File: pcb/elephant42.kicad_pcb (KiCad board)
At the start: 2 copper layers, 139.8 x 201 mm, 155 parts, among them J1 MJ-4PP-9, J3 MJ-4PP-9, J4 Conn_01x01, SW1 SW_PUSH, SW10 SW_PUSH, SW11 SW_PUSH, SW12 SW_PUSH, SW13 SW_PUSH, SW14 SW_PUSH, SW15 SW_PUSH, SW16 SW_PUSH, SW17 SW_PUSH, SW18 SW_PUSH, SW19 SW_PUSH, SW2 SW_PUSH, SW20 SW_PUSH, SW21 SW_PUSH, SW22 SW_PUSH, SW23 SW_PUSH, SW24 SW_PUSH, SW25 SW_PUSH, SW26 SW_PUSH, SW27 SW_PUSH, SW28 SW_PUSH, SW29 SW_PUSH, SW3 SW_PUSH, SW30 SW_PUSH, SW31 SW_PUSH, SW32 SW_PUSH, SW33 SW_PUSH, SW34 SW_PUSH, SW35 SW_PUSH, SW36 SW_PUSH, SW37 SW_PUSH, SW38 SW_PUSH, SW39 SW_PUSH, SW4 SW_PUSH, SW40 SW_PUSH, SW41 SW_PUSH, SW42 SW_PUSH, SW5 SW_PUSH, SW6 SW_PUSH, SW7 SW_PUSH, SW8 SW_PUSH, SW9 SW_PUSH, U1 ProMicro, U2 ProMicro

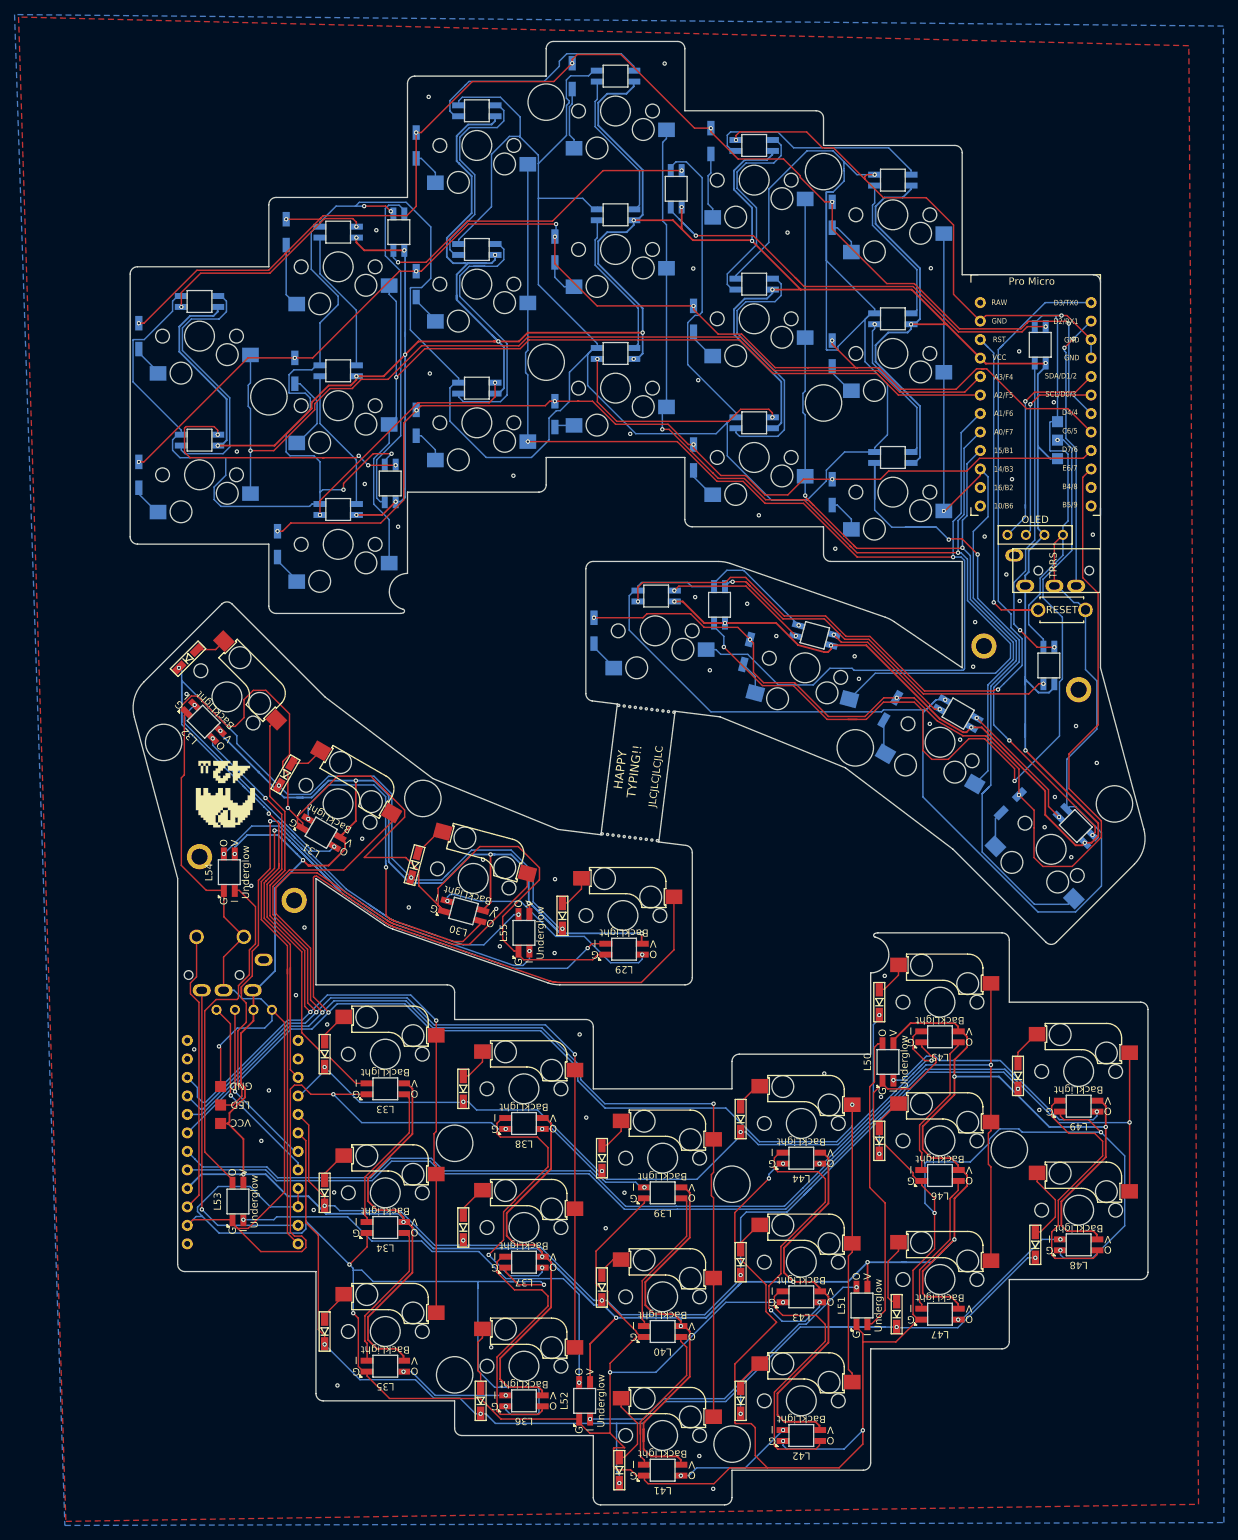
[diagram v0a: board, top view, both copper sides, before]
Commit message: Convert to choc hotswap with encoder
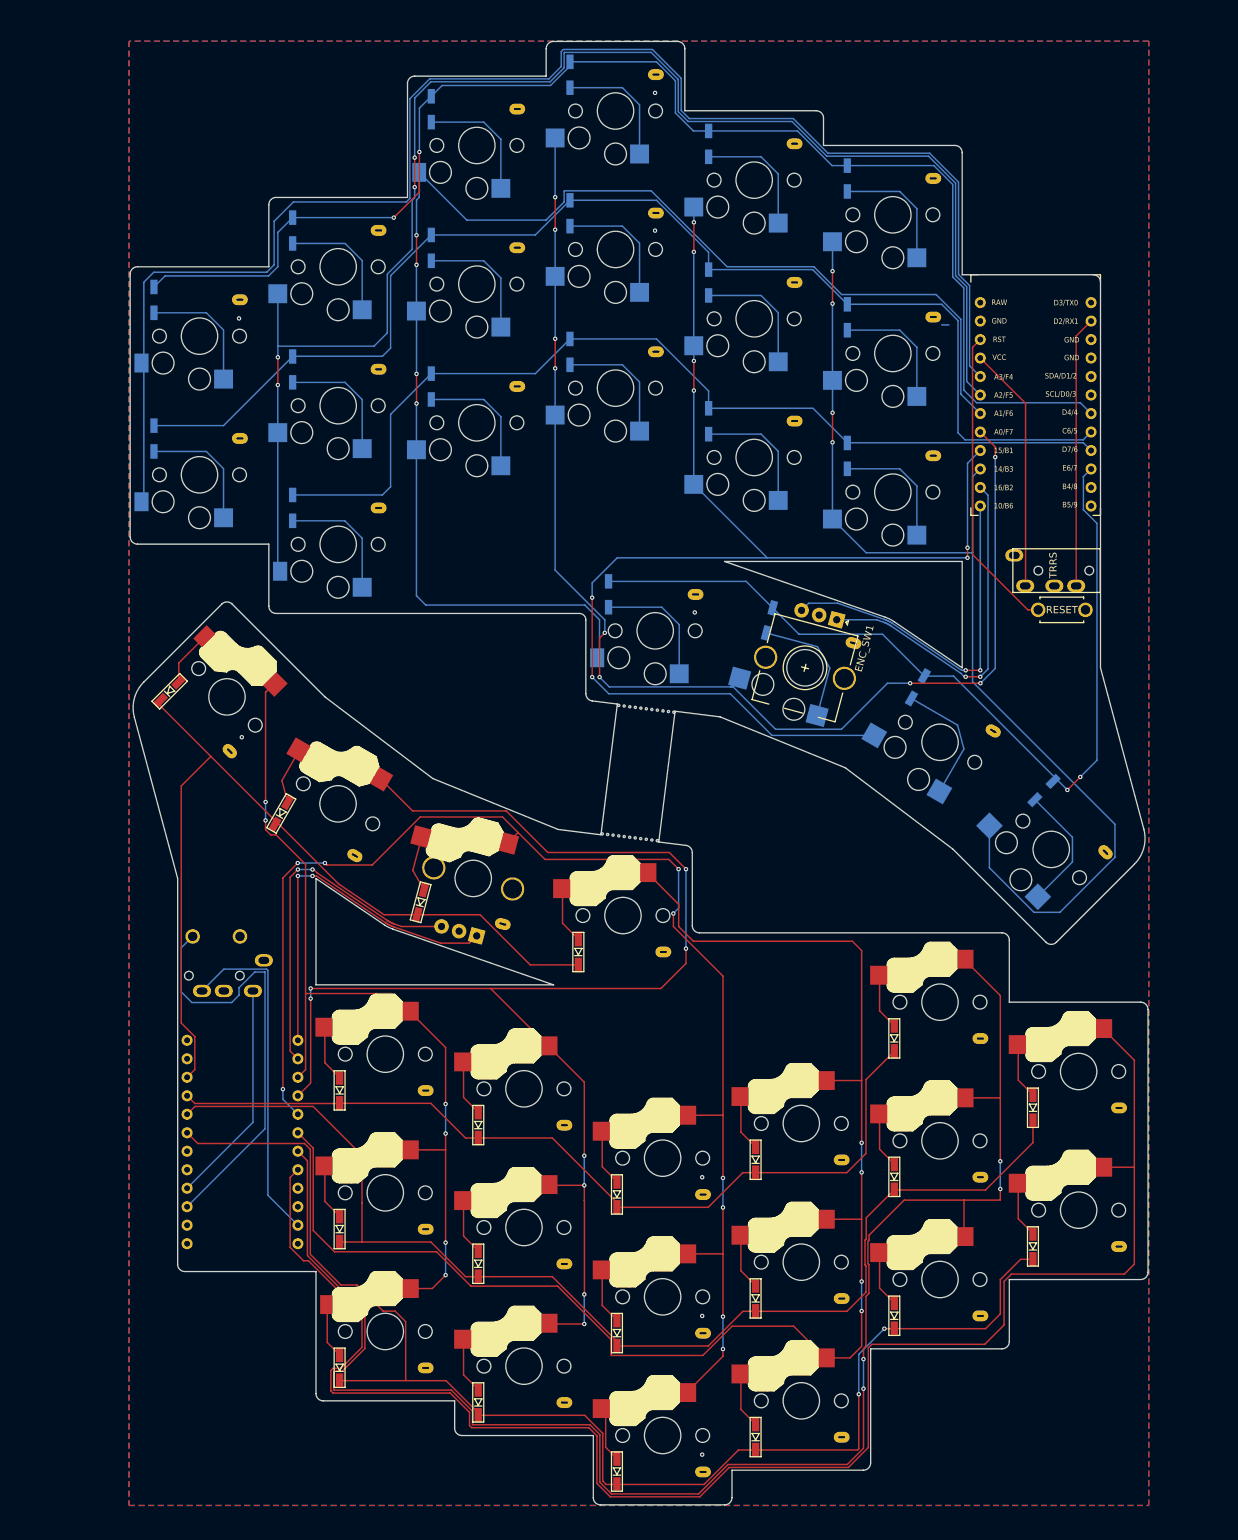
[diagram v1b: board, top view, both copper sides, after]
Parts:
- removed G***: LOGO, elephant42:icon_small
- removed G*** (x2): LOGO, elephant42:icon
- removed J4 (x4): Conn_01x01, maou_kbd:M2hole
- removed L1, L10, L11, L12, L13, L14, L15, L16, L17, L18, L19, L2, L20, L21, L29, L3, L30, L31, L32, L33, L34, L35, L36, L37, L38, L39, L4, L40, L41, L42, L43, L44, L45, L46, L47, L48, L49, L5, L6, L7, L8, L9: YS-SK6812mini-E, maou_kbd:YS-SK6812MINI-E
- removed L22, L23, L24, L25, L26, L27, L50, L51, L52, L53, L54, L55: YS-SK6812mini-E, maou_kbd:YS-SK6812MINI-E-underglow
- removed L28, L56: LED, kbd:StripLED_1side
- removed OL1, OL2: OLED, kbd:OLED_1side
- added ENC_SW1: Rotary_Encoder, Rotary_Encoder:RotaryEncoder_Alps_EC11E-Switch_Vertical_H20mm_CircularMountingHoles, F.Cu at (104.8, 98.0)
- added ENC_SW2: Rotary_Encoder, Rotary_Encoder:RotaryEncoder_Alps_EC11E-Switch_Vertical_H20mm_CircularMountingHoles, B.Cu at (59.3, 127.0)
- SW1, SW10, SW11, SW12, SW13, SW14, SW15, SW16, SW17, SW18, SW19, SW2, SW20, SW21, SW22, SW23, SW24, SW25, SW26, SW27, SW28, SW29, SW3, SW30, SW31, SW32, SW33, SW34, SW35, SW36, SW37, SW38, SW39, SW4, SW40, SW41, SW42, SW5, SW6, SW7, SW8, SW9: footprint kbd:CherryMX_Hotswap -> kbd:ChocV1_V2_Hotswap
- moved D15 8.80 mm to (72.6, 54.6)
- moved D30 6.60 mm to (79.0, 189.4)
- moved D37 5.95 mm to (98.1, 165.6)
- moved D42 5.43 mm to (73.7, 137.1)
- moved D11 5.40 mm to (91.6, 45.1)
- moved D16 5.40 mm to (91.6, 64.1)
- moved D7 5.40 mm to (15.4, 66.5)
- moved D13 5.40 mm to (34.5, 76.0)
- moved D17 5.40 mm to (110.7, 68.9)
- moved D6 5.40 mm to (110.7, 30.8)
- moved D3 5.40 mm to (53.5, 21.3)
- moved D1 5.40 mm to (15.4, 47.5)
- moved D14 5.40 mm to (53.5, 59.4)
- moved D9 5.40 mm to (53.5, 40.3)
- moved D10 5.40 mm to (72.6, 35.6)
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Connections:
- J1 pad A: (no net) -> Net-(J1-PadA)
- J3 pad A: (no net) -> Net-(J3-PadA)
- SW22 pad 1: col11 -> Net-(D22-Pad2)
- SW22 pad 2: Net-(D22-Pad2) -> col11
- SW23 pad 1: col10 -> Net-(D23-Pad2)
- SW23 pad 2: Net-(D23-Pad2) -> col10
- SW24 pad 1: col9 -> Net-(D24-Pad2)
- SW24 pad 2: Net-(D24-Pad2) -> col9
- SW25 pad 1: col8 -> Net-(D25-Pad2)
- SW25 pad 2: Net-(D25-Pad2) -> col8
- SW26 pad 1: col7 -> Net-(D26-Pad2)
- SW26 pad 2: Net-(D26-Pad2) -> col7
- SW27 pad 1: col6 -> Net-(D27-Pad2)
- SW27 pad 2: Net-(D27-Pad2) -> col6
- SW28 pad 1: col11 -> Net-(D28-Pad2)
- SW28 pad 2: Net-(D28-Pad2) -> col11
- SW29 pad 1: col10 -> Net-(D29-Pad2)
- SW29 pad 2: Net-(D29-Pad2) -> col10
- SW30 pad 1: col9 -> Net-(D30-Pad2)
- SW30 pad 2: Net-(D30-Pad2) -> col9
- SW31 pad 1: col8 -> Net-(D31-Pad2)
- SW31 pad 2: Net-(D31-Pad2) -> col8
- SW32 pad 1: col7 -> Net-(D32-Pad2)
- SW32 pad 2: Net-(D32-Pad2) -> col7
- SW33 pad 1: col6 -> Net-(D33-Pad2)
- SW33 pad 2: Net-(D33-Pad2) -> col6
- SW34 pad 1: col11 -> Net-(D34-Pad2)
- SW34 pad 2: Net-(D34-Pad2) -> col11
- SW35 pad 1: col10 -> Net-(D35-Pad2)
- SW35 pad 2: Net-(D35-Pad2) -> col10
- SW36 pad 1: col9 -> Net-(D36-Pad2)
- SW36 pad 2: Net-(D36-Pad2) -> col9
- SW37 pad 1: col8 -> Net-(D37-Pad2)
- SW37 pad 2: Net-(D37-Pad2) -> col8
- SW38 pad 1: col7 -> Net-(D38-Pad2)
- SW38 pad 2: Net-(D38-Pad2) -> col7
- SW39 pad 1: col11 -> Net-(D39-Pad2)
- SW39 pad 2: Net-(D39-Pad2) -> col11
- SW40 pad 1: col10 -> Net-(D40-Pad2)
- SW40 pad 2: Net-(D40-Pad2) -> col10
- SW41 pad 1: col9 -> Net-(D41-Pad2)
- SW41 pad 2: Net-(D41-Pad2) -> col9
- SW42 pad 1: col8 -> Net-(D42-Pad2)
- SW42 pad 2: Net-(D42-Pad2) -> col8
- U1 pad 1: led_l -> Net-(U1-Pad1)
- U1 pad 11: (no net) -> Net-(U1-Pad11)
- U1 pad 12: (no net) -> Net-(U1-Pad12)
- U1 pad 13: (no net) -> enc2
- U1 pad 14: (no net) -> enc1
- U1 pad 24: (no net) -> Net-(U1-Pad24)
- U1 pad 5: sda_l -> Net-(U1-Pad5)
- U1 pad 6: scl_l -> Net-(U1-Pad6)
- U2 pad 1: led_r -> Net-(U2-Pad1)
- U2 pad 10: row7 -> col11
- U2 pad 11: (no net) -> enc4
- U2 pad 12: (no net) -> enc3
- U2 pad 13: (no net) -> Net-(U2-Pad13)
- U2 pad 14: (no net) -> Net-(U2-Pad14)
- U2 pad 15: col11 -> row7
- U2 pad 16: col10 -> row6
- U2 pad 17: col9 -> row5
- U2 pad 18: col8 -> row4
- U2 pad 19: col7 -> Net-(U2-Pad19)
- U2 pad 20: col6 -> Net-(U2-Pad20)
- U2 pad 24: (no net) -> Net-(U2-Pad24)
- U2 pad 5: sda_r -> col6
- U2 pad 6: scl_r -> col7
- U2 pad 7: row4 -> col8
- U2 pad 8: row5 -> col9
- U2 pad 9: row6 -> col10
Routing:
- net GND: track 1649.7 -> 0.00 mm, vias 92 -> 8
- net VCC: track 1246.6 -> 64.7 mm, vias 40 -> 0
- net led_r: track 126.9 -> 0.00 mm, vias 2 -> 0
- net led_l: track 123.9 -> 0.00 mm, vias 2 -> 0
- net Net-(L27-Pad2): track 115.2 -> 0.00 mm, vias 3 -> 0
- net Net-(L55-Pad2): track 93.0 -> 0.00 mm, vias 2 -> 0
- net Net-(L4-Pad2): track 80.7 -> 0.00 mm, vias 4 -> 0
- net col1: track 126.2 -> 206.7 mm, vias 1 -> 4
- net col0: track 130.6 -> 206.8 mm, vias 1 -> 0
- net Net-(L52-Pad2): track 62.8 -> 0.00 mm, vias 2 -> 0
- net Net-(L24-Pad2): track 62.6 -> 0.00 mm, vias 2 -> 0
- net col7: track 162.2 -> 221.4 mm, vias 1 -> 4
- net Net-(L32-Pad2): track 59.0 -> 0.00 mm, vias 2 -> 0
- net col6: track 167.4 -> 223.6 mm, vias 1 -> 0
- net col4: track 119.8 -> 175.9 mm, vias 2 -> 8
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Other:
- outline, holes or cut-outs redrawn
- board text removed: "@illness072"
- board text removed: "HAPPY TYPING!!"
- board text removed: "JLCJLCJLCJLC"
- board text removed: "designed by"
- board text removed: "elephant42 v1.0"
- board text removed: "elephant42 v1.0 designed by illness072"
